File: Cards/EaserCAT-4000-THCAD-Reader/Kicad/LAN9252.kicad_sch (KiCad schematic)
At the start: 18 parts, among them U1 LAN9252_PT, Y1 25MHz

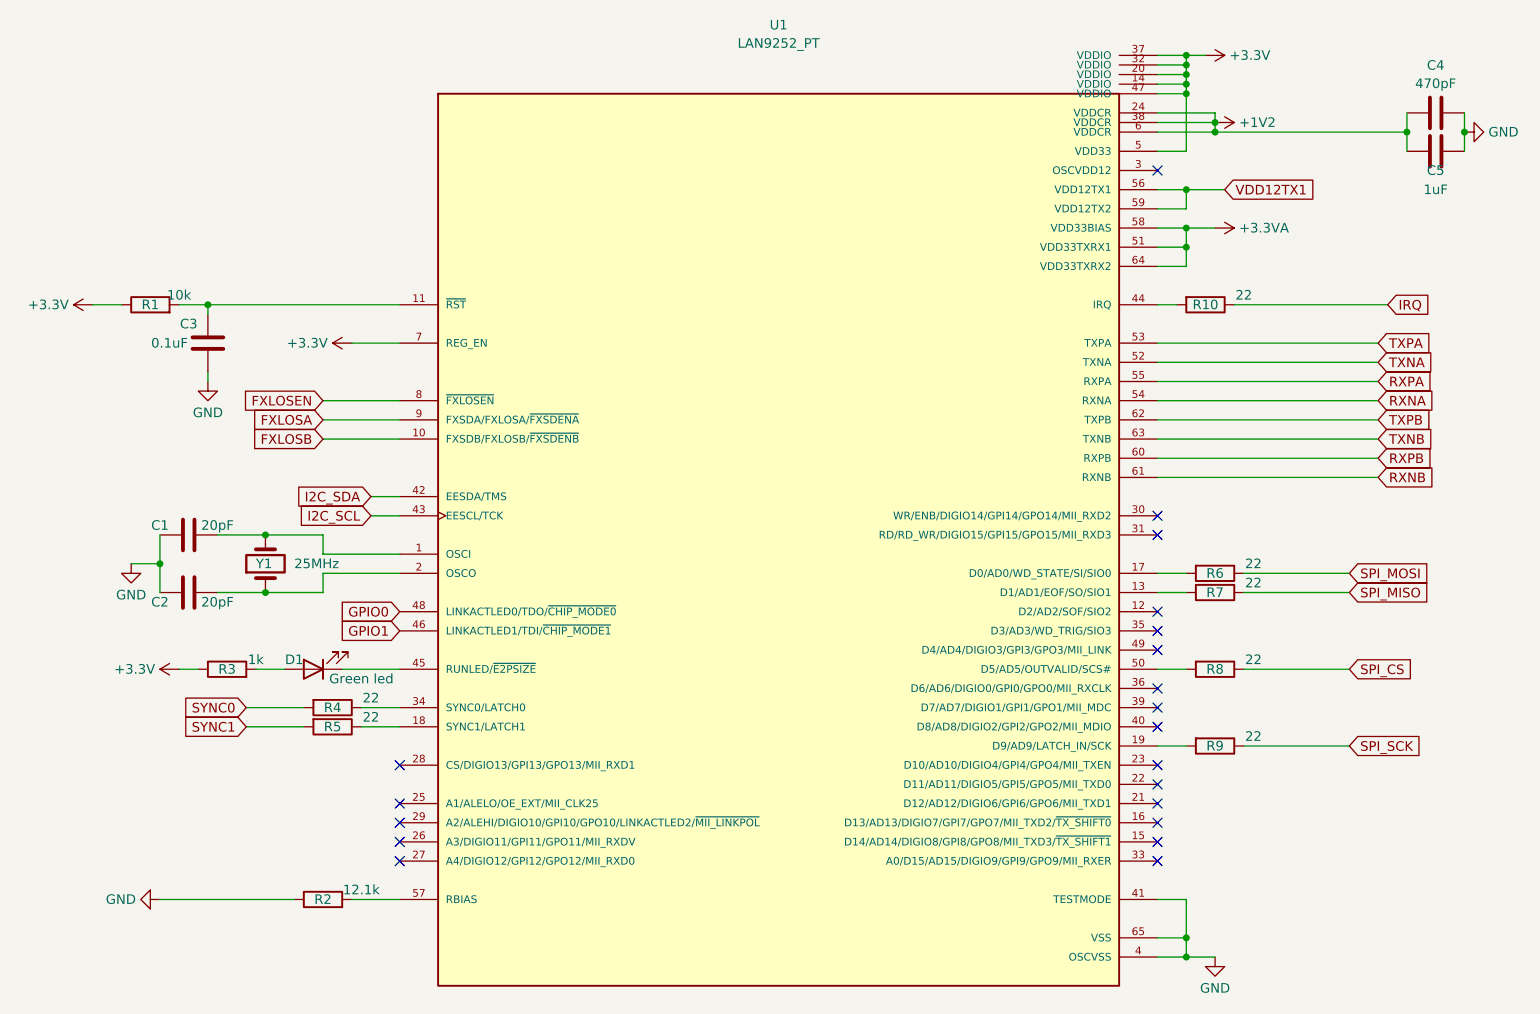
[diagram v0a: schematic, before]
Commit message: Moving all to Kicad8. Housekeeping symbols,libraries,3d-models
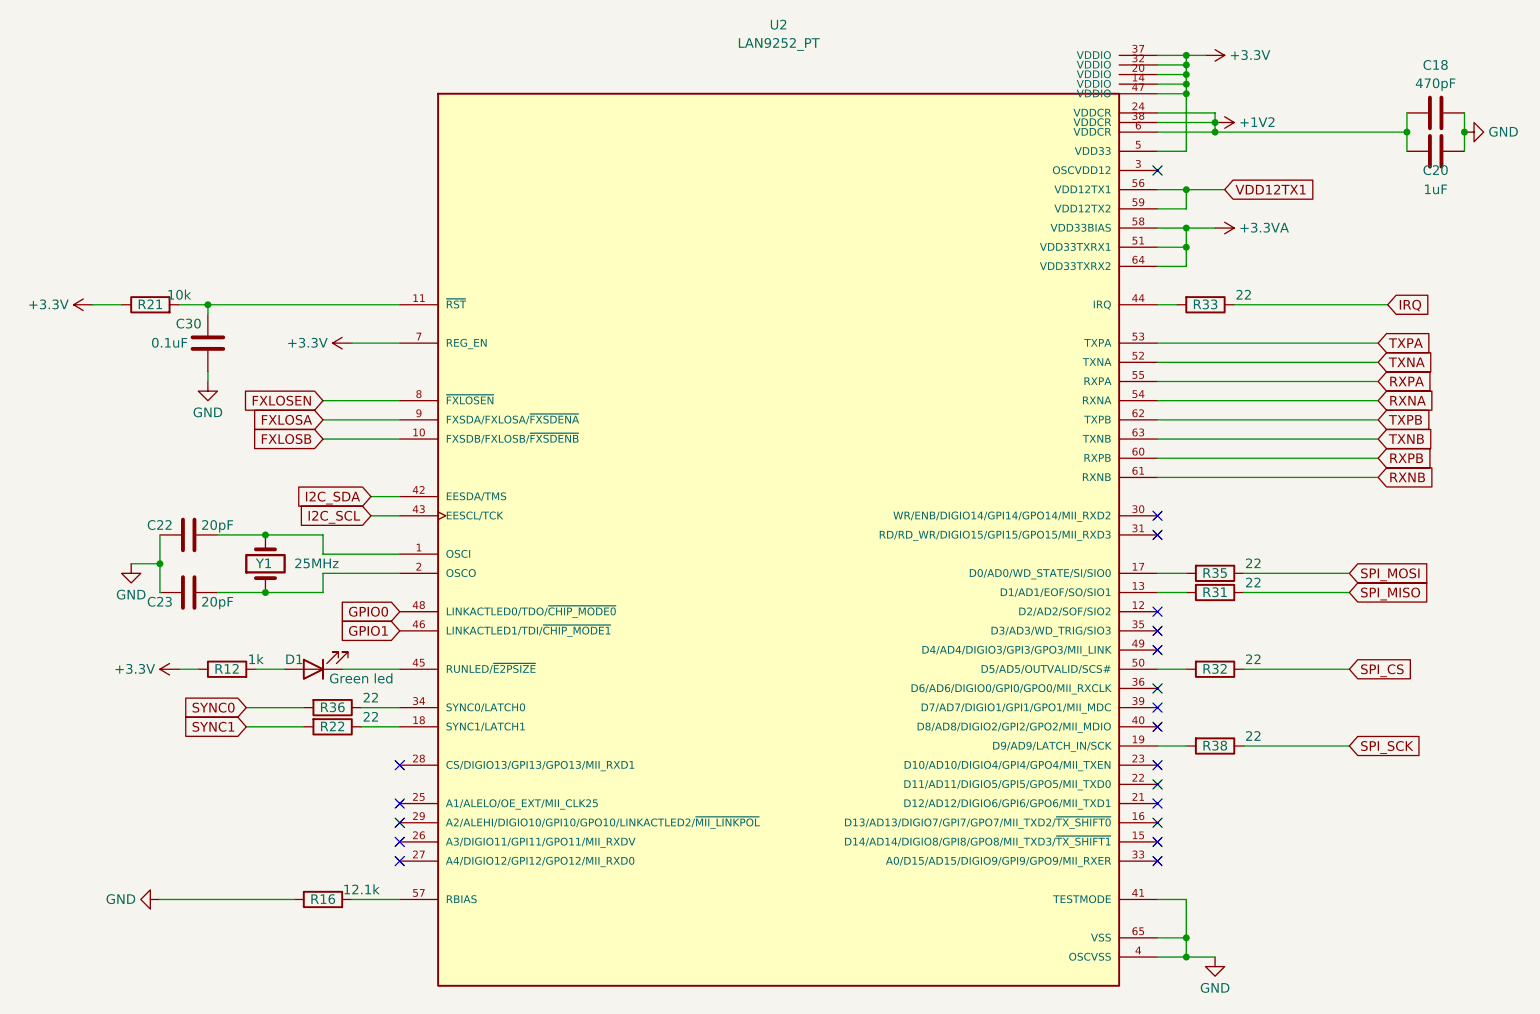
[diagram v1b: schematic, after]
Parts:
- Y1: footprint Crystal:Crystal_HC49-U_Vertical -> Crystal:Crystal_HC49-4H_Vertical
- renumbered C4 to C18, C5 to C20, C1 to C22, C2 to C23, C3 to C30, R3 to R12, R2 to R16, R1 to R21, R5 to R22, R7 to R31, R8 to R32, R10 to R33, R6 to R35, R4 to R36, R9 to R38, U1 to U2
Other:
- title: (none) -> THCAD reader
